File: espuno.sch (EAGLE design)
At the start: 34 parts, among them T1 FDN340P, U1 ADS1115IDGST, U2 NCP1117ST50T3G, U3 LP2985-33DBVR, U4 FT232R, U5 LMV358IDGKR, X1 POWERSUPPLY_DC21MMX

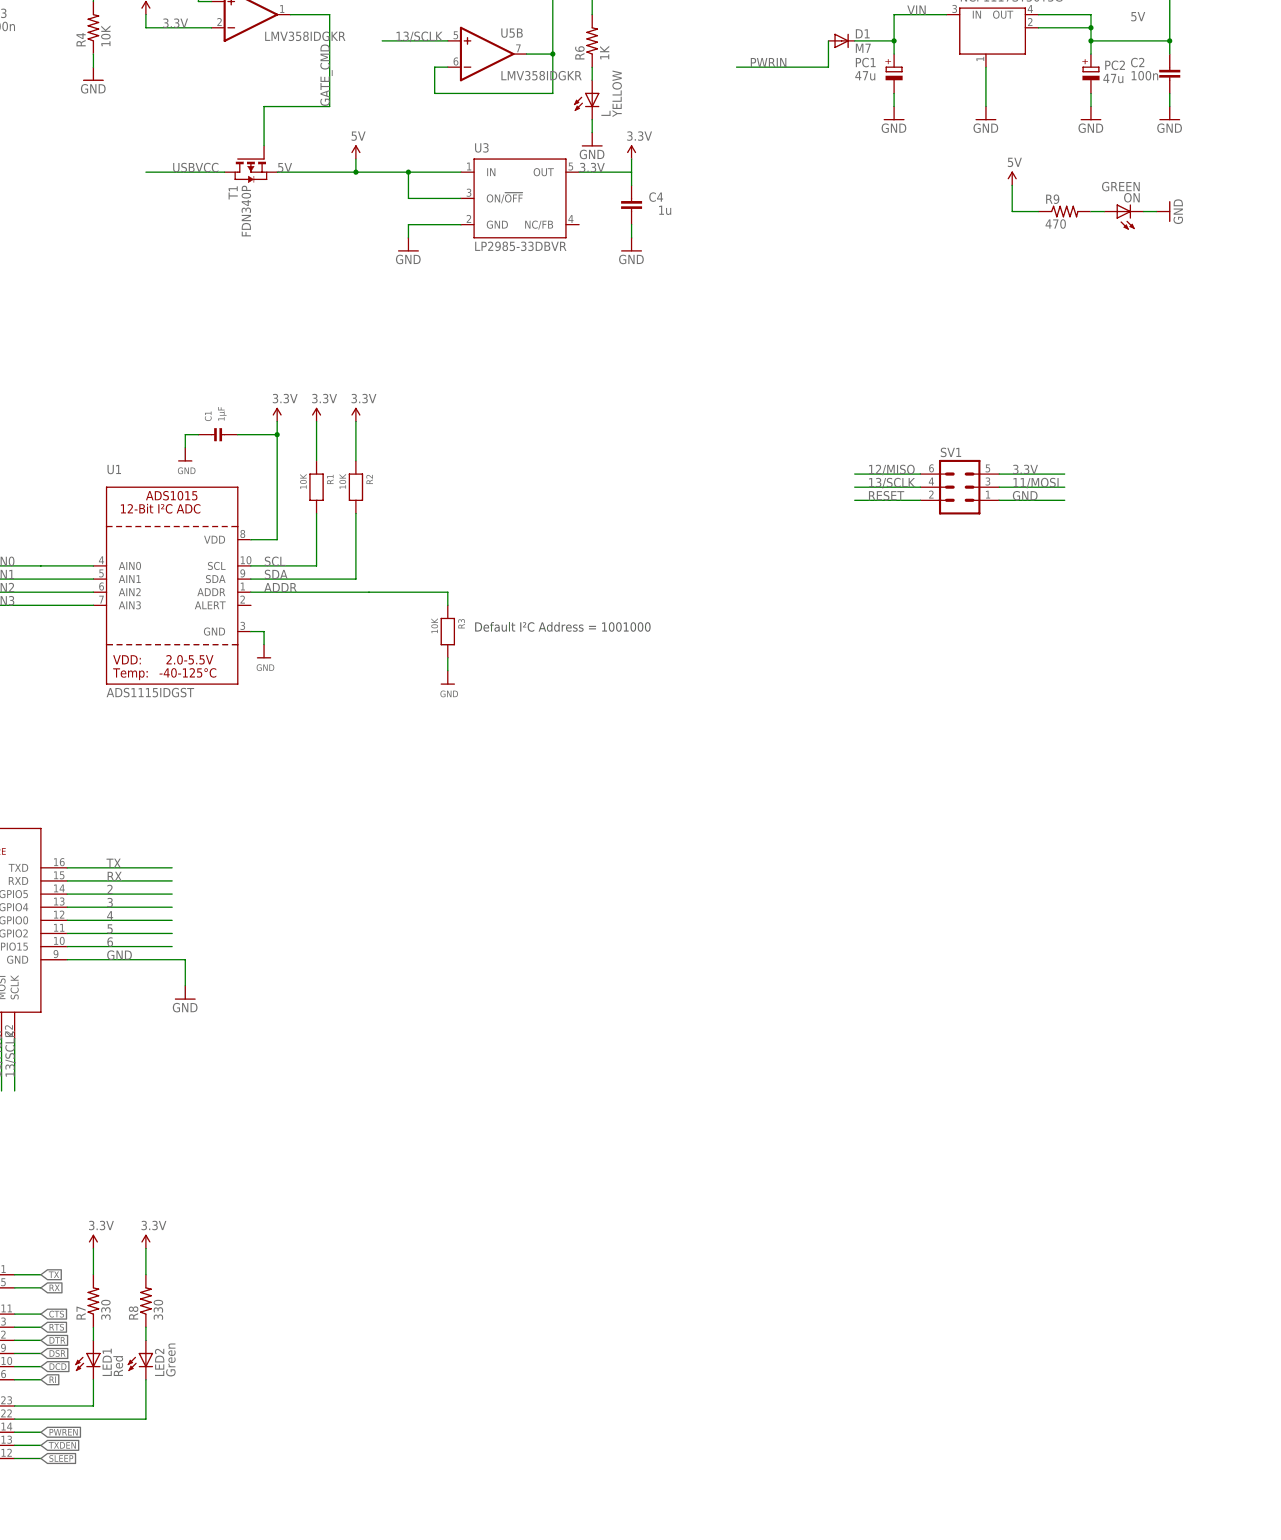
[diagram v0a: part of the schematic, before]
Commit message: Added LIPO parts, use more 0805 resistors/caps and 1206 LEDs instead of f&cking 0402s
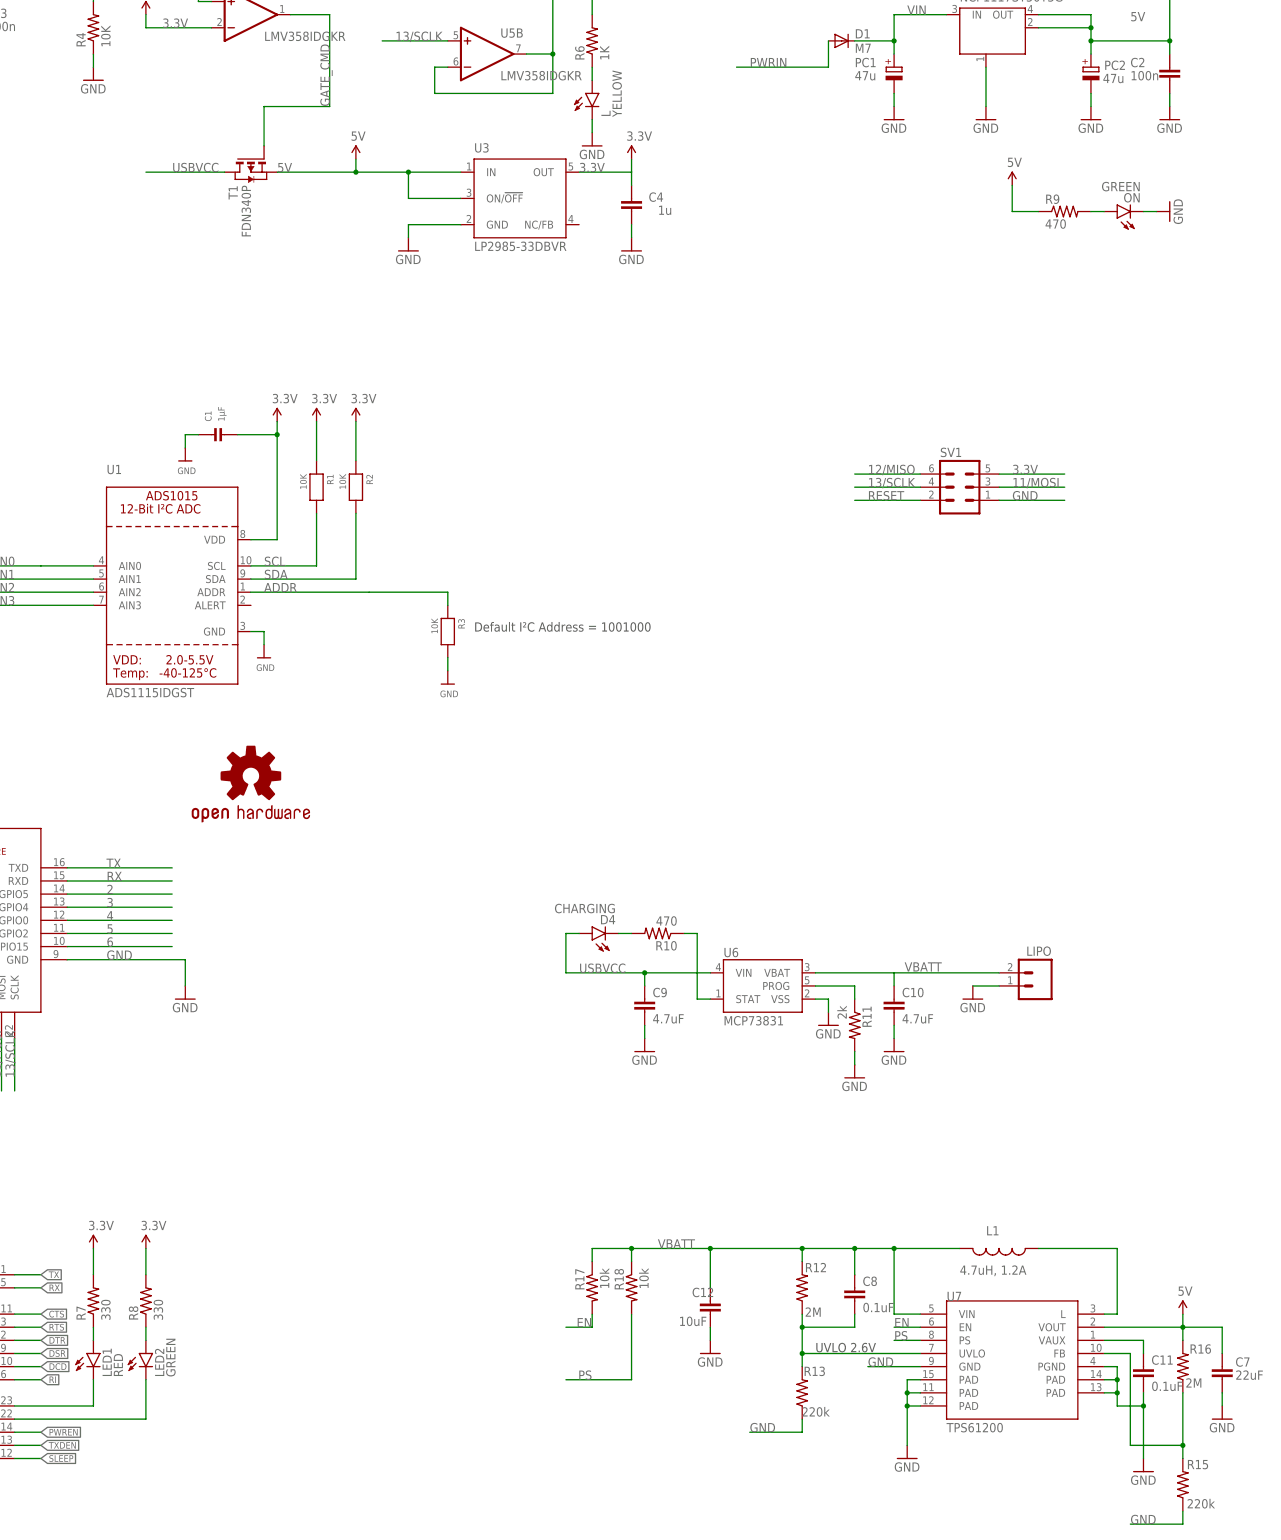
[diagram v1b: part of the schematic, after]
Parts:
- added C10, C9: 4.7uF, SparkFun-Capacitors:CAP0805
- added C11, C8: 0.1uF, SparkFun-Capacitors:CAP0805
- added C12: 10uF, SparkFun-Capacitors:CAP0805
- added C7: 22uF, SparkFun-Capacitors:CAP0805
- added D4: CHARGING, SparkFun-LED:LED1206
- added L1: 4.7uH, 1.2A, SparkFun:INDUCTOR.
- added LIPO: (no value), SparkFun-Connectors:M02JST-PTH-2
- added R10: 470, SparkFun-Resistors:RESISTOR0805-RES
- added R11: 2k, SparkFun-Resistors:RESISTOR0805-RES
- added R12, R16: 2M, SparkFun-Resistors:RESISTOR0805-RES
- added R13, R15: 220k, SparkFun-Resistors:RESISTOR0805-RES
- added R17, R18: 10k, SparkFun-Resistors:RESISTOR0805-RES
- added U$1: OSHW-LOGOS, SparkFun:OSHW-LOGOS
- added U6: MCP73831, SparkFun:MCP73831
- added U7: TPS61200, SparkFun:TPS61200
- L, ON: device led:LEDCHIP-LED0805 -> SparkFun-LED:LED1206
- LED1: value Red -> RED
- LED2: value Green -> GREEN
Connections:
- new net EN: R17.2, U7.EN
- new net FB: R15.2, R16.1, U7.FB
- new net N$11: R11.1, U6.PROG
- new net N$14: R10.1, U6.STAT
- new net N$5: L1.1, U7.L
- new net N$6: C11.1, U7.VAUX
- new net N$8: D4.C, R10.2
- new net PS: R18.2, U7.PS
- new net UVLO: C8.2, R12.1, R13.2, U7.UVLO
- new net VBATT: C10.1, C12.1, C8.1, L1.2, LIPO.2, R12.2, R17.1, R18.1, U6.VBAT, U7.VIN
- net 5V: now also C7.1, R16.2, U7.VOUT
- net GND: now also C10.2, C11.2, C12.2, C7.2, C9.2, LIPO.1, R11.2, R13.1, R15.1, U6.VSS, U7.GND, U7.PAD@1, U7.PAD@2, U7.PAD@3, U7.PAD@4, U7.PAD@5, U7.PGND
- net USBVCC: now also C9.1, D4.A, U6.VIN
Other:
- note added: "UVLO 2.6V"

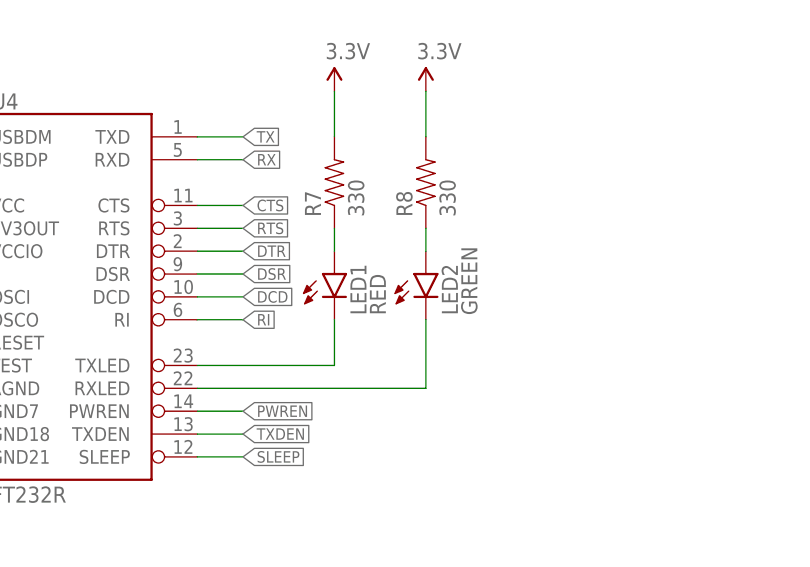
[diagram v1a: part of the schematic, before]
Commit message: Fixing layout of labels, adding ESPUNO text, slight layout tweaks to make slightly more pleasing.
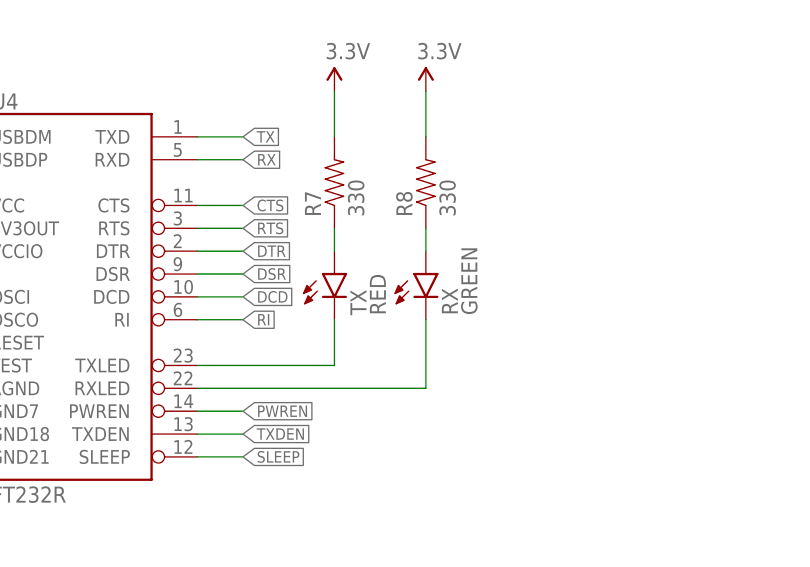
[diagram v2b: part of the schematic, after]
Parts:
- renumbered LED1 to TX, LED2 to RX
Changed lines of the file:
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@@
 <part name="R7" library="SparkFun-Resistors" deviceset="330OHM1/10W1%(0603)" device="" value="330"/>
 <part name="R8" library="SparkFun-Resistors" deviceset="330OHM1/10W1%(0603)" device="" value="330"/>
-<part name="LED1" library="SparkFun-LED" deviceset="LED-RED" device="0603" value="RED"/>
-<part name="LED2" library="SparkFun-LED" deviceset="LED-GREEN" device="0603" value="GREEN"/>
+<part name="TX" library="SparkFun-LED" deviceset="LED-RED" device="0603" value="RED"/>
+<part name="RX" library="SparkFun-LED" deviceset="LED-GREEN" device="0603" value="GREEN"/>
 <part name="SUPPLY16" library="SparkFun-Aesthetics" deviceset="3.3V" device=""/>
 <part name="SUPPLY17" library="SparkFun-Aesthetics" deviceset="3.3V" device=""/>
@@
 <instance part="R7" gate="G$1" x="129.54" y="-50.8" rot="R90"/>
 <instance part="R8" gate="G$1" x="139.7" y="-50.8" rot="R90"/>
-<instance part="LED1" gate="G$1" x="129.54" y="-60.96"/>
-<instance part="LED2" gate="G$1" x="139.7" y="-60.96"/>
+<instance part="TX" gate="G$1" x="129.54" y="-60.96"/>
+<instance part="RX" gate="G$1" x="139.7" y="-60.96"/>
 <instance part="SUPPLY16" gate="G$1" x="129.54" y="-40.64"/>
 <instance part="SUPPLY17" gate="G$1" x="139.7" y="-40.64"/>
@@
 <wire x1="129.54" y1="-71.12" x2="129.54" y2="-66.04" width="0.1524" layer="91"/>
 <pinref part="U4" gate="G$1" pin="TXLED"/>
-<pinref part="LED1" gate="G$1" pin="C"/>
+<pinref part="TX" gate="G$1" pin="C"/>
 </segment>
 </net>
@@
 <wire x1="139.7" y1="-73.66" x2="139.7" y2="-66.04" width="0.1524" layer="91"/>
 <pinref part="U4" gate="G$1" pin="RXLED"/>
-<pinref part="LED2" gate="G$1" pin="C"/>
+<pinref part="RX" gate="G$1" pin="C"/>
 </segment>
 </net>
@@
 <wire x1="129.54" y1="-55.88" x2="129.54" y2="-58.42" width="0.1524" layer="91"/>
 <pinref part="R7" gate="G$1" pin="1"/>
-<pinref part="LED1" gate="G$1" pin="A"/>
+<pinref part="TX" gate="G$1" pin="A"/>
 </segment>
 </net>
@@
 <wire x1="139.7" y1="-55.88" x2="139.7" y2="-58.42" width="0.1524" layer="91"/>
 <pinref part="R8" gate="G$1" pin="1"/>
-<pinref part="LED2" gate="G$1" pin="A"/>
-</segment>
-</net>
+<pinref part="RX" gate="G$1" pin="A"/>
+</segment>
+</net>

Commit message: Espuno Mk2, with bigass 1206's for errything
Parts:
- removed PCB1: ARDUINO_UNO, E14_Arduino_revB:ARDUINO_UNO
- removed SJ1: JUMPER-PAD-2-NC_BY_TRACE, SparkFun-Passives:JUMPER-PAD-2-NC_BY_TRACE
- added FLASH, RESET: (no value), switch-omron:10-XX
- added GND_GPIO15: (no value), SparkFun-Retired:JUMPER-2PTH_LOCK
- added J1: ARDUINO_R3_SHIELD, SparkFun-Boards:ARDUINO_R3_SHIELD
- added JP1: USB-SMD-NS, SparkFun-Connectors:USB-SMD-NS
- added PC3: 47u, rcl:CPOL-EUD
- C10, C11, C12, C7, C8, C9: device SparkFun-Capacitors:CAP0805 -> rcl:C-EUC1206K
- C2, C3, C4: device SmartPrj:C-EU0603-RND -> rcl:C-EUC1206K
- C5: device SparkFun-Capacitors:0.1UF-25V(+80/-20%)(0603) -> rcl:C-EUC1206K
- C6: device SparkFun-Capacitors:10UF-16V-10%(TANT) -> rcl:CPOL-EUSMCA
- R1, R2, R3: device microbuilder:RESISTOR0805 -> rcl:R-EU_M1206
- R10, R11, R12, R13, R15, R16, R17, R18: device SparkFun-Resistors:RESISTOR0805-RES -> rcl:R-EU_M1206
- R4, R5: device SparkFun-Resistors:10KOHM-1/10W-1%(0603)0603 -> rcl:R-EU_M1206
- R6: device SparkFun-Resistors:1KOHM-1/10W-1%(0603) -> rcl:R-EU_M1206
- R7, R8: device SparkFun-Resistors:330OHM1/10W1%(0603) -> rcl:R-EU_M1206
- R9: device SparkFun-Resistors:470OHM1/10W1%(0603) -> rcl:R-EU_M1206
- RX: device SparkFun-LED:LED-GREEN0603 -> SparkFun-LED:LED1206
- TX: device SparkFun-LED:LED-RED0603 -> SparkFun-LED:LED1206
- renumbered PC2 to PC4
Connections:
- removed net N$10: PCB1.<USB>GND, SJ1.1
- removed net RXLED: RX.C, U4.RXLED
- removed net TXLED: TX.C, U4.TXLED
- new net AIN4: J1.A5
- new net N$7: R7.1, U4.RXLED
- new net N$9: R8.1, U4.TXLED
- net 10: now also J1.*D10; no longer PCB1.~10
- net 11/MOSI: now also J1.*D11; no longer PCB1.~11
- net 12/MISO: now also J1.D12; no longer PCB1.12
- net 13/SCLK: now also J1.D13; no longer PCB1.13
- net 2: now also J1.D2; no longer PCB1.2
- net 3: now also J1.*D3; no longer PCB1.~3
- net 3.3V: now also J1.3.3V, PC1.+, RX.A, TX.A; no longer PCB1.3.3V, R7.2, R8.2
- net 4: now also FLASH.P, FLASH.P1, J1.D4; no longer PCB1.4
- net 5: now also J1.*D5; no longer PCB1.~5
- net 5V: now also J1.5V; no longer PCB1.5V
- net 6: now also GND_GPIO15.1, J1.*D6; no longer PCB1.~6
- net 7: now also J1.D7; no longer PCB1.7
- net 8: now also J1.D8; no longer PCB1.8
- net 9: now also J1.*D9; no longer PCB1.~9
- net ADC: now also J1.A0; no longer PCB1.A0
- net AIN0: now also J1.A1; no longer PCB1.A1
- net AIN1: now also J1.A2; no longer PCB1.A2
- net AIN2: now also J1.A3; no longer PCB1.A3
- net AIN3: now also J1.A4; no longer PCB1.A4
- net GND: now also FLASH.S, FLASH.S1, GND_GPIO15.2, J1.GND@0, J1.GND@1, J1.GND@2, JP1.GND, PC3.-, R6.1, RESET.S, RESET.S1; no longer L.C, PCB1.<PWR>-V, PCB1.A5, PCB1.GND, PCB1.GND., PCB1.GND.., SJ1.2
- net L13: now also L.A; no longer R6.2
- net N$2: now also L.C, R6.2; no longer L.A, R6.1
- net N$3: now also R7.2, RX.C; no longer R7.1, TX.A
- net N$4: now also R8.2, TX.C; no longer R8.1, RX.A
- net PWRIN: no longer PCB1.<PWR>+V
- net RESET: now also J1.RES, RESET.P, RESET.P1; no longer PCB1.RESET
- net RX: now also J1.RX; no longer PCB1.0(RX)
- net SCL: now also J1.SCL; no longer PCB1.28(SCL)
- net SDA: now also J1.SDA; no longer PCB1.27(SDA)
- net TX: now also J1.TX; no longer PCB1.1(TX)
- net USBVCC: now also JP1.VBUS; no longer PCB1.<USB>+V
- net USB_D+: now also JP1.D+; no longer PCB1.<USB>D+
- net USB_D-: now also JP1.D-; no longer PCB1.<USB>D-
- net VIN: now also J1.VIN, PC3.+; no longer PC1.+, PCB1.VIN
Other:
- moved on the sheet: C10, C11, C12, C5, C7, C8, C9, L, PC1, RX, T1, TX

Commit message: Mk2 revision complete. Tidied schematics and board. Added pullups.
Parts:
- removed GND_GPIO15: (no value), SparkFun-Retired:JUMPER-2PTH_LOCK
- removed SJ2: JUMPER-PAD-2-NC_BY_TRACE, SparkFun-Passives:JUMPER-PAD-2-NC_BY_TRACE
- removed U$1: OSHW-LOGOS, SparkFun:OSHW-LOGOS
- added FRAME1, FRAME2: (no value), SparkFun-Aesthetics:FRAME-LETTERNO_PACKAGE
- added LOGO1: OSHW-LOGOS, SparkFun-Aesthetics:OSHW-LOGOS
- added R14, R19, R20, R21: 10k, SparkFun-Resistors:RESISTOR1206
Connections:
- net 10 renamed 10/GPIO12
- net 2 renamed 2/GPIO5
- net 3 renamed 3/GPIO4
- net 5 renamed 5/GPIO2
- net 7 renamed 7/GPIO10
- net 8 renamed 8/GPIO9
- net 9 renamed 9/GPIO13
- net SCL renamed SCL/GPIO14
- net SDA renamed SDA/GPIO16
- removed net 4: FLASH.P, FLASH.P1, J1.D4, MDL1.GPIO0
- removed net 6: GND_GPIO15.1, J1.*D6, MDL1.GPIO15
- removed net DTR: U4.DTR
- removed net RTS: U4.RTS
- new net 4/GPIO0: FLASH.P, FLASH.P1, J1.D4, MDL1.GPIO0, R20.2, U4.DTR
- new net 6/GPIO15: J1.*D6, MDL1.GPIO15, R21.2
- net 3.3V: now also R14.1, R19.1, R20.1; no longer SJ2.2
- net CH_PD: now also R19.2; no longer SJ2.1
- net GND: now also R21.1; no longer GND_GPIO15.2
- net RESET: now also R14.2, U4.RTS
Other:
- note added: "ADC"
- note added: "Board IO"
- note added: "Boost Converter"
- note added: "LiPo Charger"
- note added: "Power Caps"
- note added: "Power LED"
- note added: "Powersupply switching"
- note added: "Processor ESP8266 12F"
- note added: "Programmer"
- note added: "Pullups"
- note added: "Regulator 12v => 5v"
- note added: "Regulator 5v => 3.3v"
- note added: "pin 13 "L" lamp equivilent"
- moved on the sheet: C1, C10, C11, C12, C2, C3, C4, C5, C6, C7, C8, C9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

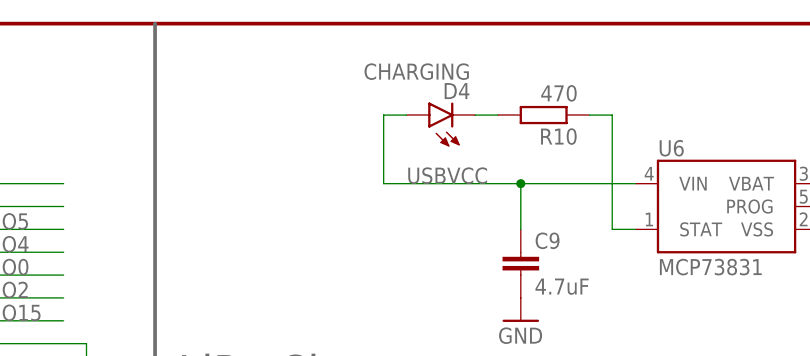
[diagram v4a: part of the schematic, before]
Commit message: Move some labels, change 'CHARGING' into 'CHRG' for brevity
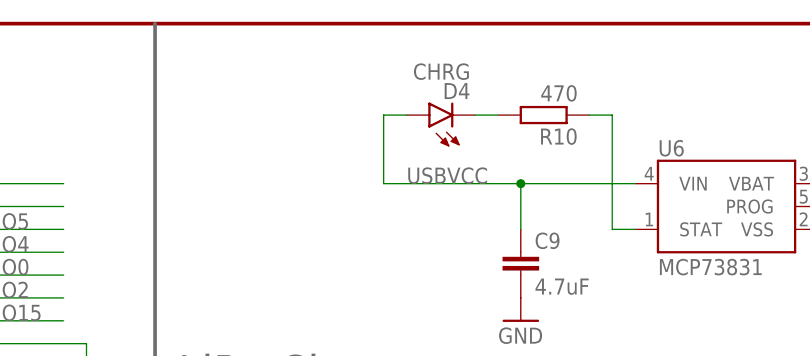
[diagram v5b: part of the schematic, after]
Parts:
- D4: value CHARGING -> CHRG
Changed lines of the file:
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@@
 <part name="GND5" library="supply1" deviceset="GND" device=""/>
 <part name="GND13" library="supply1" deviceset="GND" device=""/>
-<part name="D4" library="SparkFun-LED" deviceset="LED" device="1206" value="CHARGING"/>
+<part name="D4" library="SparkFun-LED" deviceset="LED" device="1206" value="CHRG"/>
 <part name="R10" library="rcl" deviceset="R-EU_" device="M1206" value="470"/>
 <part name="U6" library="SparkFun" deviceset="MCP73831" device=""/>
